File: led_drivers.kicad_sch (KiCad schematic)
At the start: 23 parts, among them IC1 SamacSys_Parts_HT16K33-28SOP, IC2 SamacSys_Parts_HT16K33-28SOP, SW1 SW_Omron_B3FS, SW2 SW_Omron_B3FS, SW3 SW_Omron_B3FS, SW4 SW_Omron_B3FS

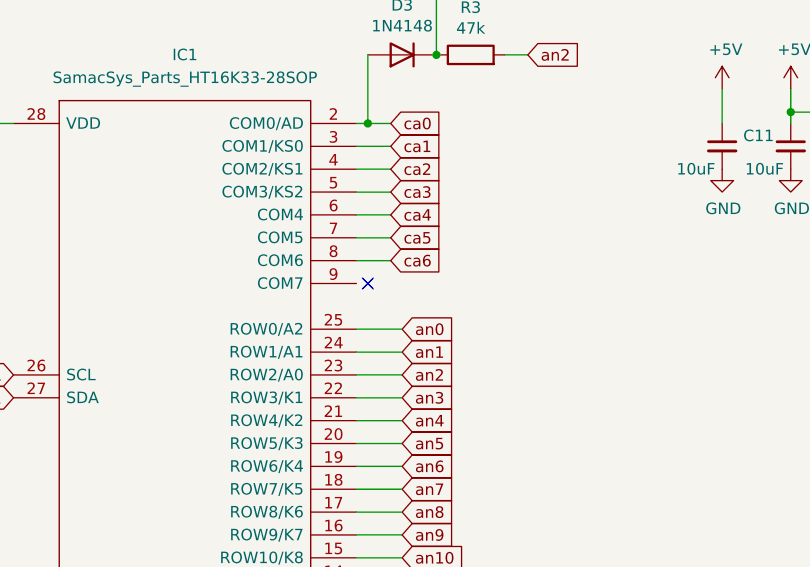
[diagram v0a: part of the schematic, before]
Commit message: Add second decimal connection to first led driver
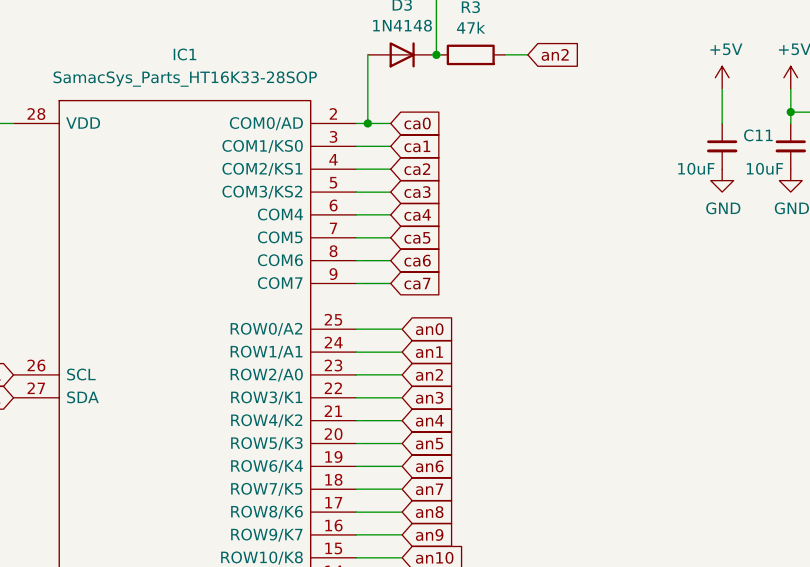
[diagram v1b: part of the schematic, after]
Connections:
- net ca7: now reaches IC1.9 (COM7)
- no-connect marks 1 -> 0
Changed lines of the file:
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@@
   (junction (at 106.68 149.86) (diameter 0) (color 0 0 0 0)
   )
-  (no_connect (at 93.98 71.12))
   (wire (pts (xy 140.97 49.53) (xy 140.97 52.07))
     (stroke (width 0) (type default))
@@
   )
   (wire (pts (xy 222.25 92.71) (xy 205.74 92.71))
+    (stroke (width 0) (type default))
+  )
+  (wire (pts (xy 92.71 71.12) (xy 96.52 71.12))
     (stroke (width 0) (type default))
   )
@@
     )
   )
+  (global_label "ca7" (shape input) (at 96.52 71.12 0) (fields_autoplaced)
+    (effects (font (size 1.27 1.27)) (justify left))
+    (property "Intersheetrefs" "${INTERSHEET_REFS}" (at 102.9523 71.12 0)
+      (effects (font (size 1.27 1.27)) (justify left) hide)
+    )
+  )

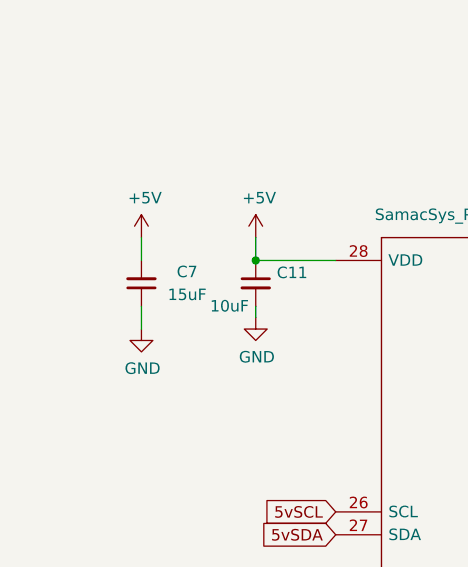
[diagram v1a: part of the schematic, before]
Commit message: Update ltp305 footprint
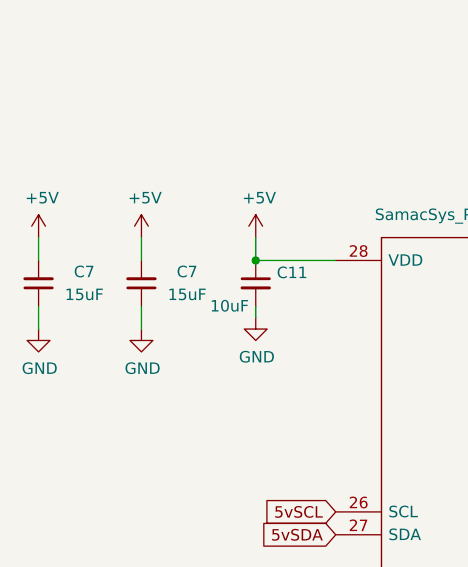
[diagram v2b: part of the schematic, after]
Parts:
- added C7: 15uF, Capacitor_SMD:C_1210_3225Metric_Pad1.33x2.70mm_HandSolder, symbol Device:C_Small
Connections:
- net +5V: now also C7.2
- net GND: now also C7.1
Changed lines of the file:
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@@
+    (stroke (width 0) (type default))
+  )
+  (wire (pts (xy 21.59 58.42) (xy 21.59 60.96))
     (stroke (width 0) (type default))
   )
@@
   )
   (wire (pts (xy 109.22 38.1) (xy 111.76 38.1))
+    (stroke (width 0) (type default))
+  )
+  (wire (pts (xy 21.59 50.8) (xy 21.59 53.34))
     (stroke (width 0) (type default))
   )
@@
     )
   )
+  (symbol (lib_id "power:+5V") (at 21.59 50.8 0) (unit 1)
+    (in_bom yes) (on_board yes) (dnp no)
+    (property "Reference" "#PWR08" (at 21.59 54.61 0)
+      (effects (font (size 1.27 1.27)) hide)
+    )
+    (property "Value" "+5V" (at 21.971 46.4058 0)
+      (effects (font (size 1.27 1.27)))
+    )
+    (property "Footprint" "" (at 21.59 50.8 0)
+      (effects (font (size 1.27 1.27)) hide)
+    )
+    (property "Datasheet" "" (at 21.59 50.8 0)
+      (effects (font (size 1.27 1.27)) hide)
+    )
+    (pin "1")
+    (instances
+      (project "LTP305_ESP32_CLOCK"
+        (path "/c007e288-8439-49d9-bbdf-49724c34958c"
+          (reference "#PWR08") (unit 1)
+        )
+      )
+      (project "ltp_kikad"
+        (path "/eed35b77-cbf9-4596-9b17-2558f81058ba"
+          (reference "#PWR04") (unit 1)
+        )
+        (path "/eed35b77-cbf9-4596-9b17-2558f81058ba/7d22e16e-a0ba-4766-b1de-c8cbb28f14f7"
+          (reference "#PWR030") (unit 1)
+        )
+      )
+    )
+  )
   (symbol (lib_id "Switch:SW_Omron_B3FS") (at 93.98 139.7 0) (unit 1)
     (in_bom yes) (on_board yes) (dnp no)
@@
         (path "/eed35b77-cbf9-4596-9b17-2558f81058ba/7d22e16e-a0ba-4766-b1de-c8cbb28f14f7"
           (reference "SW2") (unit 1)
+        )
+      )
+    )
+  )
+  (symbol (lib_id "Device:C_Small") (at 21.59 55.88 180) (unit 1)
+    (in_bom yes) (on_board yes) (dnp no)
+    (property "Reference" "C7" (at 26.67 54.61 0)
+      (effects (font (size 1.27 1.27)))
+    )
+    (property "Value" "15uF" (at 26.67 57.15 0)
+      (effects (font (size 1.27 1.27)))
+    )
+    (property "Footprint" "Capacitor_SMD:C_1210_3225Metric_Pad1.33x2.70mm_HandSolder" (at 21.59 55.88 0)
+      (effects (font (size 1.27 1.27)) hide)
+    )
+    (property "Datasheet" "~" (at 21.59 55.88 0)
+      (effects (font (size 1.27 1.27)) hide)
+    )
+    (pin "1")
+    (pin "2")
+    (instances
+      (project "LTP305_ESP32_CLOCK"
+        (path "/c007e288-8439-49d9-bbdf-49724c34958c"
+          (reference "C7") (unit 1)
+        )
+      )
+      (project "ltp_kikad"
+        (path "/eed35b77-cbf9-4596-9b17-2558f81058ba"
+          (reference "C6") (unit 1)
+        )
+        (path "/eed35b77-cbf9-4596-9b17-2558f81058ba/eeffdcd2-f49f-4c6e-9443-50950813e7b1"
+          (reference "C10") (unit 1)
+        )
+        (path "/eed35b77-cbf9-4596-9b17-2558f81058ba/7d22e16e-a0ba-4766-b1de-c8cbb28f14f7"
+          (reference "C17") (unit 1)
         )
       )
@@
         )
       )
+    )
+  )
+  (symbol (lib_id "power:GND") (at 21.59 60.96 0) (unit 1)
+    (in_bom yes) (on_board yes) (dnp no)
+    (property "Reference" "#PWR033" (at 21.59 67.31 0)
+      (effects (font (size 1.27 1.27)) hide)
+    )
+    (property "Value" "GND" (at 21.717 65.3542 0)
+      (effects (font (size 1.27 1.27)))
+    )
+    (property "Footprint" "" (at 21.59 60.96 0)
+      (effects (font (size 1.27 1.27)) hide)
+    )
+    (property "Datasheet" "" (at 21.59 60.96 0)
+      (effects (font (size 1.27 1.27)) hide)
+    )
+    (pin "1")
+    (instances
+      (project "LTP305_ESP32_CLOCK"
+        (path "/c007e288-8439-49d9-bbdf-49724c34958c"
+          (reference "#PWR033") (unit 1)
+        )
+      )
+      (project "ltp_kikad"
+        (path "/eed35b77-cbf9-4596-9b17-2558f81058ba"
+          (reference "#PWR09") (unit 1)
+        )
+        (path "/eed35b77-cbf9-4596-9b17-2558f81058ba/eeffdcd2-f49f-4c6e-9443-50950813e7b1"
+          (reference "#PWR035") (unit 1)
+        )
+        (path "/eed35b77-cbf9-4596-9b17-2558f81058ba/7d22e16e-a0ba-4766-b1de-c8cbb28f14f7"
+          (reference "#PWR047") (unit 1)
+        )
+      )

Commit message: Piatnag_5_bt
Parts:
- added R3: 47k, Resistor_SMD:R_0603_1608Metric, symbol Device:R
- added SW4: SW_Omron_B3FS, Button_Switch_SMD:SW_SPST_Omron_B3FS-105xP, symbol Switch:SW_Omron_B3FS
- C11: footprint Capacitor_SMD:C_0603_1608Metric -> Capacitor_SMD:C_0805_2012Metric_Pad1.18x1.45mm_HandSolder
- D3: footprint Diode_SMD:D_SOD-523 -> Diode_SMD:D_0805_2012Metric
- SW1: renamed from SW2; footprint Button_Switch_THT:SW_PUSH_6mm_H4.3mm -> Button_Switch_SMD:SW_SPST_Omron_B3FS-105xP
- SW2: renamed from SW1; footprint Button_Switch_THT:SW_PUSH_6mm_H4.3mm -> Button_Switch_SMD:SW_SPST_Omron_B3FS-105xP
- SW3: footprint Button_Switch_THT:SW_PUSH_6mm_H4.3mm -> Button_Switch_SMD:SW_SPST_Omron_B3FS-105xP
- SW5: renamed from SW4; footprint Button_Switch_THT:SW_PUSH_6mm_H4.3mm -> Button_Switch_SMD:SW_SPST_Omron_B3FS-105xP
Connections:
- net 2_an11: now also R3.2
- net sw_ks2: now also SW4.1
- new net: R3.1, SW4.2
